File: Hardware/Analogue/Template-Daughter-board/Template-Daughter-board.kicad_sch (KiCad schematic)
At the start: 6 parts, among them J1 Audio In, J2 Audio Out, J3 Digital Pass Through, J4 Digital In, J5 Power Out, J6 Power In

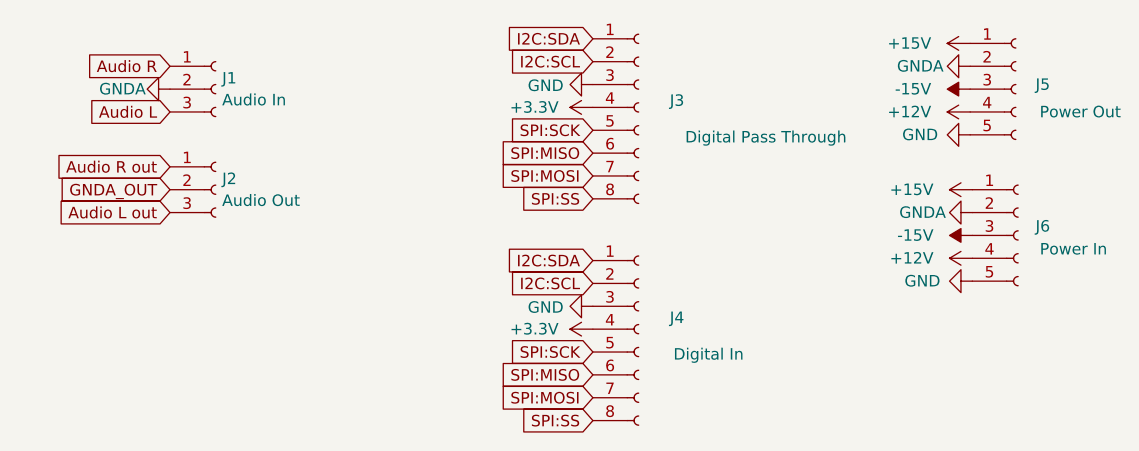
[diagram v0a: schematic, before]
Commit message: Updated Template-Daughter-board to reflect changes
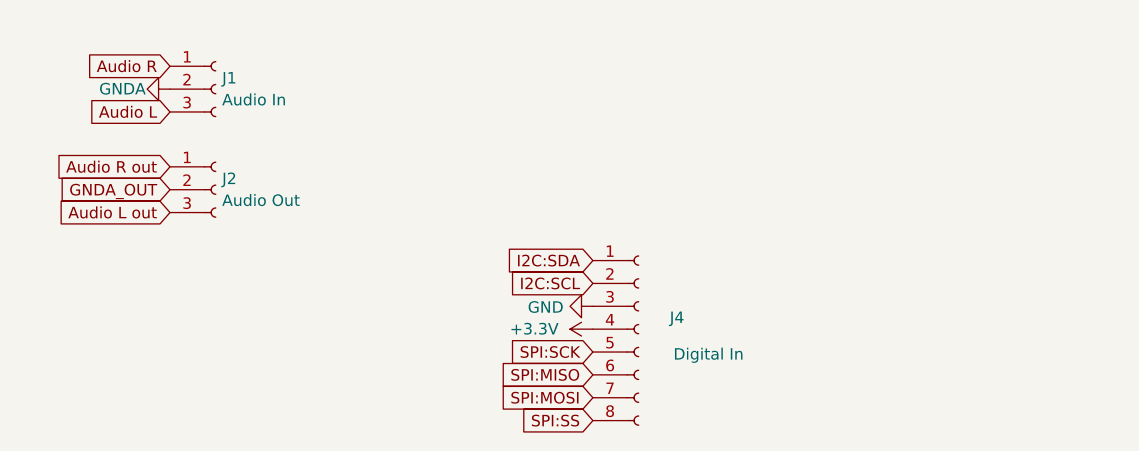
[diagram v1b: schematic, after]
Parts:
- removed J3: Digital Pass Through, Connector_JST:JST_XH_B8B-XH-A_1x08_P2.50mm_Vertical, symbol Connector:Conn_01x08_Female
- removed J5: Power Out, Connector_JST:JST_XH_B5B-XH-A_1x05_P2.50mm_Vertical, symbol Connector:Conn_01x05_Female
- removed J6: Power In, Connector_PinHeader_2.54mm:PinHeader_1x05_P2.54mm_Vertical, symbol Connector:Conn_01x05_Female
